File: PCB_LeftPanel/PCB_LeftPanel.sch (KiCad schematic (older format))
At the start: 26 parts, among them J1 USB_B, J2 AVR-ISP-6, J3 Jack-DC, U1 ATmega16-16PU, U2 7442, U3 MCP2200-I-SO, Y1 Crystal

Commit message: Add files via upload
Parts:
- J1: symbol Connector:USB_B -> PCB_LeftPanel-rescue:USB_B-Connector
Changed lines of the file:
@@
 	4250 1750 4250 1850
 $Comp
-L Connector:USB_B J1
+L PCB_LeftPanel-rescue:USB_B-Connector J1
 U 1 1 6129CE8A
 P 1400 1150

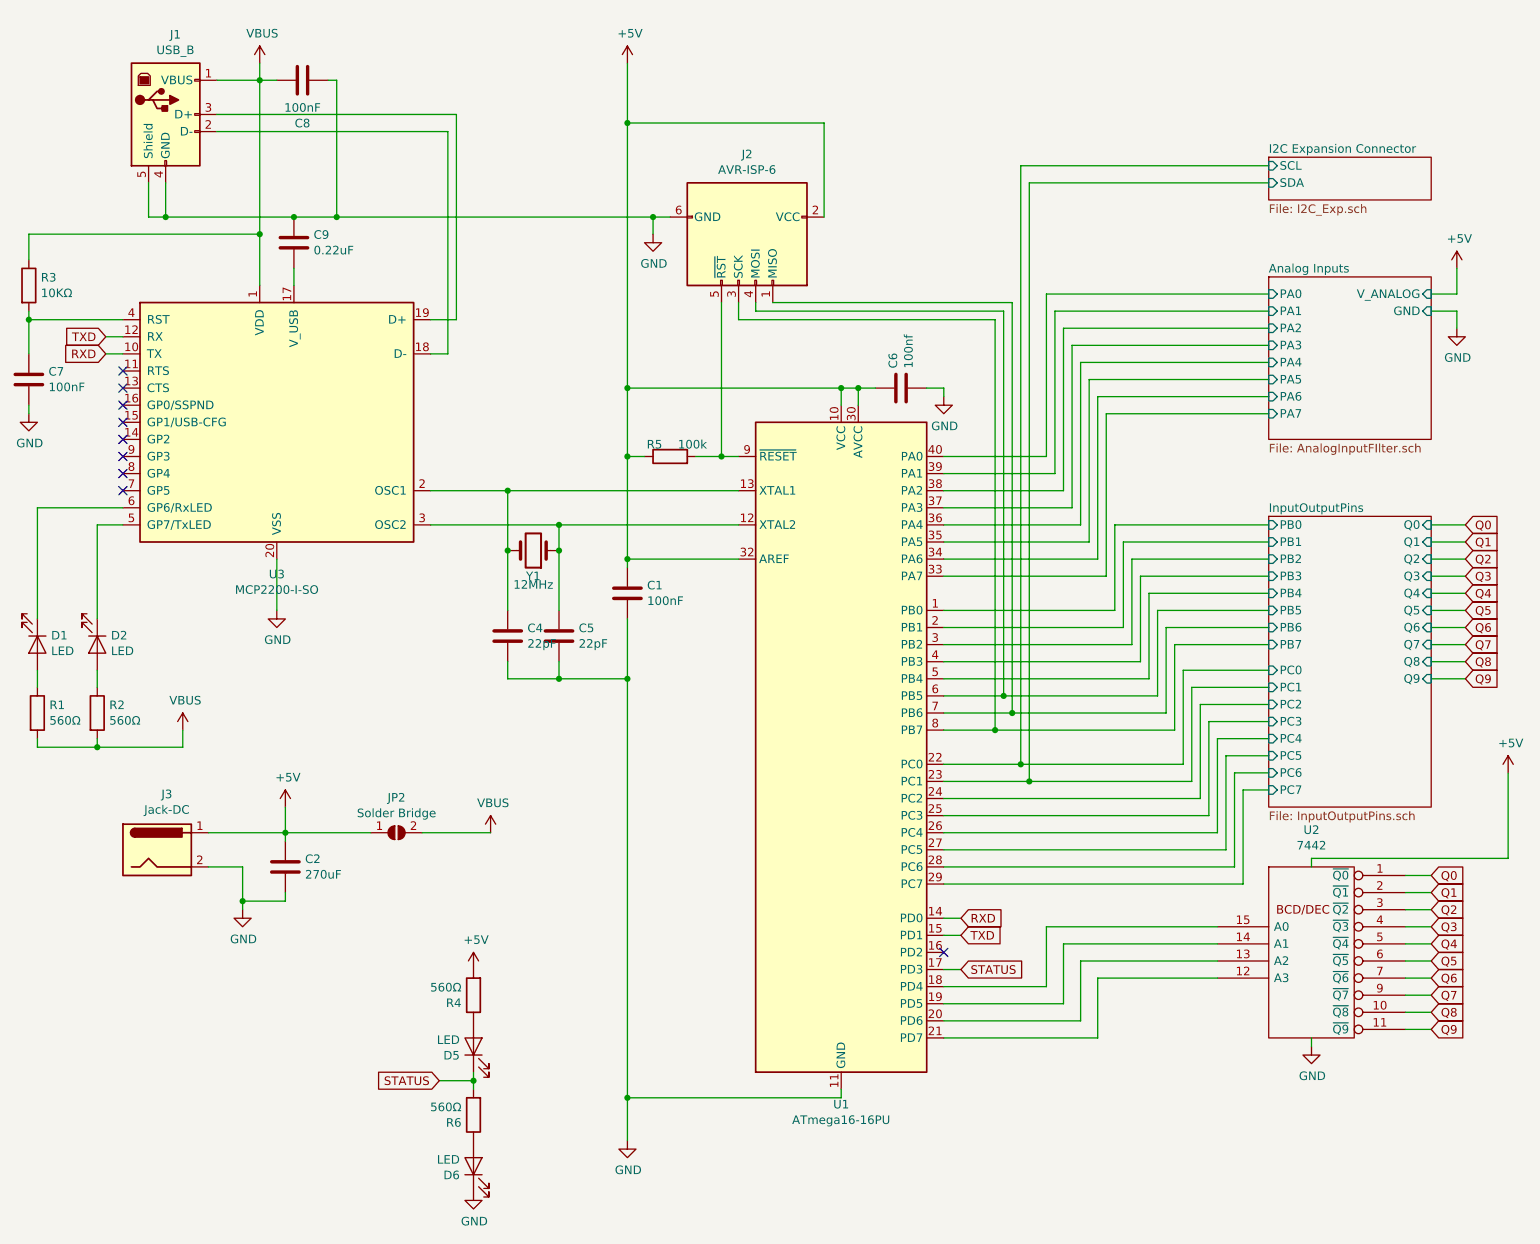
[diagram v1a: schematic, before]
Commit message: Add files via upload
Update to Revision 4.A
Board now based on Arduino Leonardo / Uno
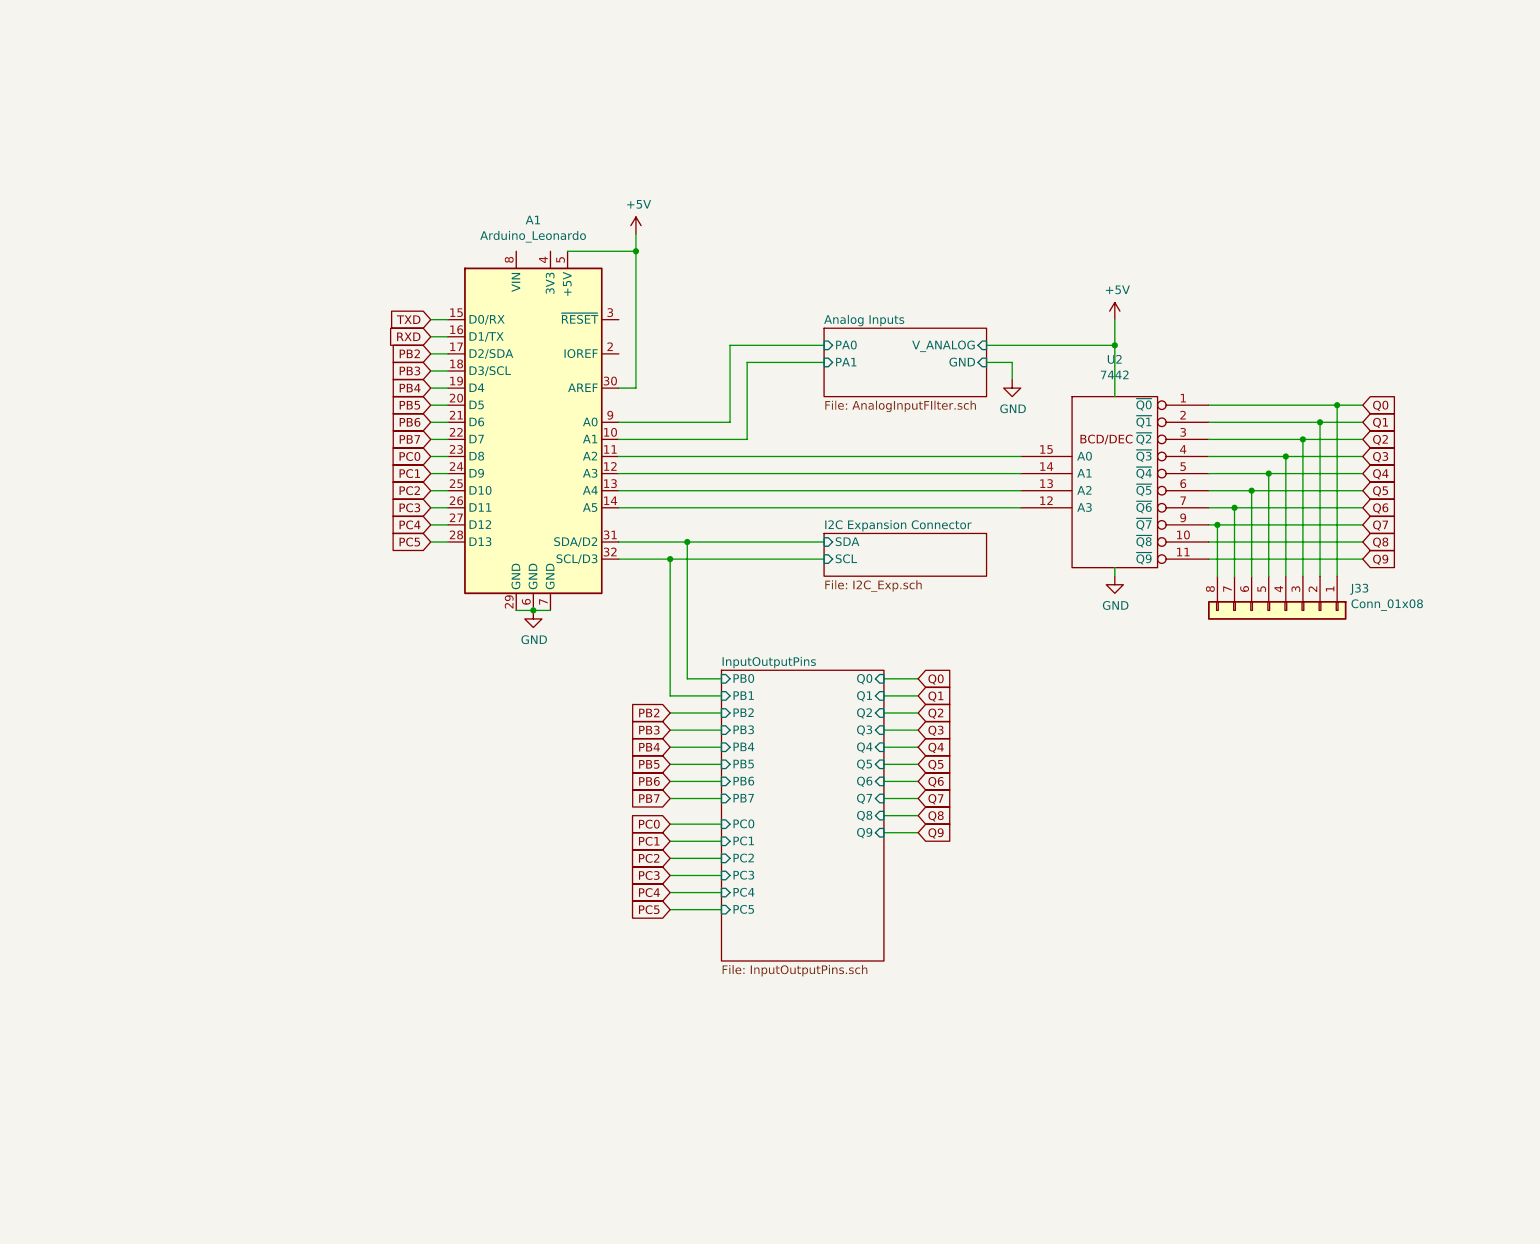
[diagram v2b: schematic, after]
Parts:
- removed C1, C7, C8: 100nF, Capacitor_THT:CP_Radial_D8.0mm_P5.00mm, symbol Device:C
- removed C2: 270uF, Capacitor_THT:CP_Radial_D8.0mm_P5.00mm, symbol Device:C
- removed C4, C5: 22pF, Capacitor_THT:CP_Radial_D8.0mm_P5.00mm, symbol Device:C
- removed C6: 100nf, Capacitor_THT:CP_Radial_D8.0mm_P5.00mm, symbol Device:C
- removed C9: 0.22uF, Capacitor_THT:CP_Radial_D8.0mm_P5.00mm, symbol Device:C
- removed D1, D2, D5, D6: LED, LED_THT:LED_D3.0mm, symbol Device:LED
- removed J1: USB_B, Connector_USB:USB_B_OST_USB-B1HSxx_Horizontal, symbol PCB_LeftPanel-rescue:USB_B-Connector
- removed J2: AVR-ISP-6, Connector_PinHeader_2.00mm:PinHeader_2x03_P2.00mm_Vertical, symbol Connector:AVR-ISP-6
- removed J3: Jack-DC, Connector_BarrelJack:BarrelJack_CUI_PJ-063AH_Horizontal, symbol Connector:Jack-DC
- removed JP2: Solder Bridge, Jumper:SolderJumper-2_P1.3mm_Open_Pad1.0x1.5mm, symbol Jumper:SolderJumper_2_Open
- removed R1, R2, R4, R6: 560Ω, Resistor_THT:R_Axial_DIN0204_L3.6mm_D1.6mm_P7.62mm_Horizontal, symbol Device:R
- removed R3: 10KΩ, Resistor_THT:R_Axial_DIN0204_L3.6mm_D1.6mm_P7.62mm_Horizontal, symbol Device:R
- removed R5: 100k, Resistor_THT:R_Axial_DIN0204_L3.6mm_D1.6mm_P7.62mm_Horizontal, symbol Device:R
- removed U1: ATmega16-16PU, Package_DIP:DIP-40_W15.24mm, symbol MCU_Microchip_ATmega:ATmega16-16PU
- removed U3: MCP2200-I-SO, Package_SO:SOIC-20W_7.5x12.8mm_P1.27mm, symbol Interface_USB:MCP2200-I-SO
- removed Y1: Crystal, Crystal:Crystal_HC49-4H_Vertical, symbol Device:Crystal
- added A1: Arduino_Leonardo, Module:Arduino_UNO_R3, symbol MCU_Module:Arduino_Leonardo
- added J33: Conn_01x08, Connector_PinHeader_2.54mm:PinHeader_1x08_P2.54mm_Vertical, symbol Connector_Generic:Conn_01x08
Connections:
- net +5V: now also A1.30 (AREF), A1.5 (+5V)
- net Analog Inputs/PA0: now also A1.9 (A0)
- net Analog Inputs/PA1: now also A1.10 (A1)
- net GND: now also A1.29 (GND), A1.6 (GND), A1.7 (GND)
- net I2C Expansion Connector/SCL: now also A1.32 (SCL/D3)
- net I2C Expansion Connector/SDA: now also A1.31 (SDA/D2)
- net Q0: now also J33.1 (Pin_1)
- net Q1: now also J33.2 (Pin_2)
- net Q2: now also J33.3 (Pin_3)
- net Q3: now also J33.4 (Pin_4)
- net Q4: now also J33.5 (Pin_5)
- net Q5: now also J33.6 (Pin_6)
- net Q6: now also J33.7 (Pin_7)
- net Q7: now also J33.8 (Pin_8)
- net RXD: now also A1.16 (D1/TX)
- net TXD: now also A1.15 (D0/RX)
- net at U2.15 (A0): now also A1.11 (A2)
- net at U2.14 (A1): now also A1.12 (A3)
- net at U2.13 (A2): now also A1.13 (A4)
- net at U2.12 (A3): now also A1.14 (A5)
- new net PB2: A1.17 (D2/SDA)
- new net PB3: A1.18 (D3/SCL)
- new net PB4: A1.19 (D4)
- new net PB5: A1.20 (D5)
- new net PB6: A1.21 (D6)
- new net PB7: A1.22 (D7)
- new net PC0: A1.23 (D8)
- new net PC1: A1.24 (D9)
- new net PC2: A1.25 (D10)
- new net PC3: A1.26 (D11)
- new net PC4: A1.27 (D12)
- new net PC5: A1.28 (D13)
- no-connect marks 9 -> 0
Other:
- moved on the sheet: U2
